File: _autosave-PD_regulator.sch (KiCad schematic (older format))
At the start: 25 parts, among them J5 Switch, J6 Fast_Out, U5 ADA4896-2ARMZ, U8 ADG1413, U9 LTC6228xS8

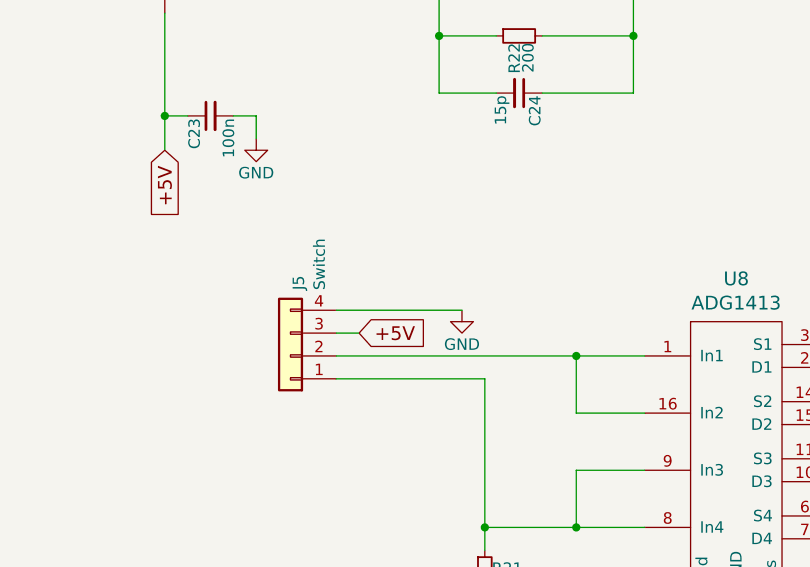
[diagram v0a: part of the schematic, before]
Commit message: Add fast PD regulator
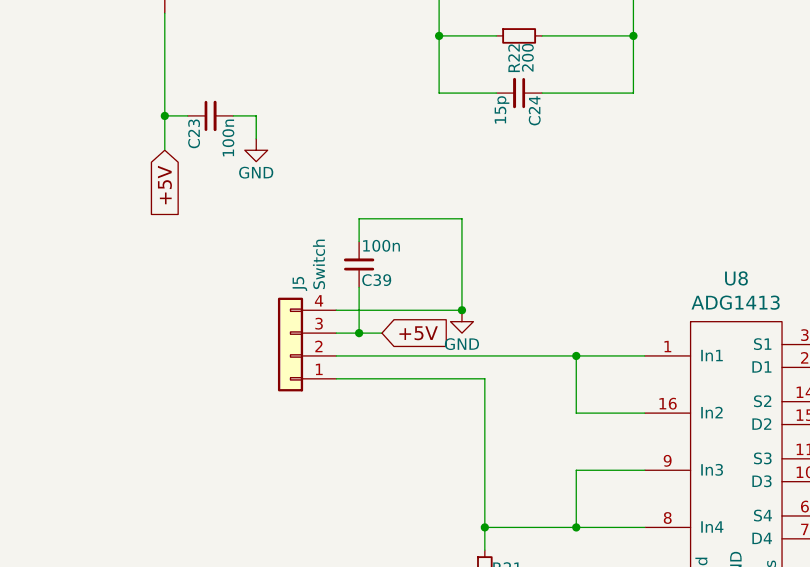
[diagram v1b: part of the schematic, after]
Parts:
- added C39: 100n, Capacitor_SMD:C_0603_1608Metric, symbol Device:C_Small
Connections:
- net +5V: now also C39.1
- net GND: now also C39.2
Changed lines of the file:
@@
 Wire Wire Line
 	8800 2400 8700 2400
-Text GLabel 3150 4350 2    60   Input ~ 0
+Text GLabel 3250 4350 2    60   Input ~ 0
 +5V
 $Comp
@@
 Wire Wire Line
 	3150 4350 3050 4350
+$Comp
+L Device:C_Small C39
+U 1 1 61E8ECDD
+P 3150 4050
+F 0 "C39" H 3160 4120 50  0000 L CNN
+F 1 "100n" H 3160 3970 50  0000 L CNN
+F 2 "Capacitor_SMD:C_0603_1608Metric" H 3150 4050 50  0001 C CNN
+F 3 "" H 3150 4050 50  0001 C CNN
+	1    3150 4050
+	1    0    0    1
+$EndComp
+Wire Wire Line
+	3150 4150 3150 4350
+Wire Wire Line
+	3150 4350 3250 4350
+Connection ~ 3150 4350
+Wire Wire Line
+	3150 3950 3150 3850
+Wire Wire Line
+	3150 3850 3600 3850
+Wire Wire Line
+	3600 3850 3600 4250
+Connection ~ 3600 4250
 $EndSCHEMATC
